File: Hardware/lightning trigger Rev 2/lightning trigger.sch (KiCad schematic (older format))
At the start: 55 parts, among them J1 Conn_01x02, J2 Conn_02x03_Odd_Even, J3 Conn_01x04, J4 PJ-237-6A, J5 PJ-237-6A, J6 USB_OTG, J7 Conn_01x01, J8 Conn_01x01, Q1 Q_Photo_NPN, Q2 BC846B_215, SW1 SW_SPDT, U1 MCP6001, U10 MCP4532, U2 MCP4532, U3 ATMEGA328P-AU, U5 LTV-827S, U6 FS8205, U7 FS312F-G, U8 TP4056, U9 LTV-827S, Y1 Crystal

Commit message: updating resistors and capacitors to be macrofab house parts
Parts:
- removed D1: Green LED, LEDs:LED_0805, symbol Device:LED
- removed D2: Red LED, LEDs:LED_0805, symbol Device:LED
- removed J1: Conn_01x02, Connector_PinHeader_1.00mm:PinHeader_1x02_P1.00mm_Vertical, symbol conn:Conn_01x02
- removed R15, R16, R17: 1k, Resistor_SMD:R_0805_2012Metric, symbol Device:R
- removed R5, R6, R7: 150, Resistor_SMD:R_0805_2012Metric, symbol Device:R
- removed S1: K1-5203UA-01, K1-5203UA-01:K1-5203UA-01, symbol k1-5203ua-01:K1-5203UA-01
- added U4: HM-11, symbol HM-11:HM-11
- C1, C5, C6, C7, C8, C9: footprint Capacitors_SMD:C_0805 -> Capacitor_SMD:C_0603_1608Metric; Manufacturer (none) -> KEMET; Manufacturer P/N 0805B104K250 -> C0603C104J5RACTU; Supplier LCSC -> (none); Supplier P/N C128353 -> (none)
- C10, C4: footprint Capacitors_SMD:C_0805 -> Capacitor_SMD:C_0603_1608Metric; Manufacturer (none) -> KEMET; Manufacturer P/N N/A -> C0603C102J1RACTU; Supplier N/A -> Macrofab; Supplier P/N N/A -> MF-CAP-0603-1nF
- C2, C3: footprint Capacitors_SMD:C_0805 -> Capacitor_SMD:C_0603_1608Metric; Manufacturer (none) -> KEMET; Manufacturer P/N N/A -> C0603C220J1GACTU; Supplier N/A -> Macrofab; Supplier P/N N/A -> MF-CAP-0603-22pF
- J6: footprint USB_Micro:USB_Micro_C77238 -> (none)
- R1: footprint Resistor_SMD:R_0805_2012Metric -> Resistor_SMD:R_0603_1608Metric; Manufacturer (none) -> Panasonic; Manufacturer P/N RMCF0805FT10K0 -> ERJ-3GEYJ103V; Supplier Digikey -> Macrofab; Supplier P/N RMCF0805FT10K0CT-ND -> MF-RES-0603-10K
- R10, R11, R18, R19, R2, R9: footprint Resistor_SMD:R_0805_2012Metric -> Resistor_SMD:R_0603_1608Metric; Manufacturer (none) -> Panasonic; Manufacturer P/N RNCP0603FTD150R -> ERJ-3GEYJ151V; Supplier Digikey -> (none); Supplier P/N RNCP0603FTD150RCT-ND -> (none)
- R12, R13, R14: value 1k -> 2k; footprint Resistor_SMD:R_0805_2012Metric -> Resistor_SMD:R_0603_1608Metric; Manufacturer (none) -> Panasonic; Manufacturer P/N RS-05K1001FT -> ERJ-3GEYJ202V; Supplier LCSC -> (none); Supplier P/N C115316 -> (none)
- R3, R4: value 150 -> 10k; footprint Resistor_SMD:R_0805_2012Metric -> Resistor_SMD:R_0603_1608Metric; Manufacturer (none) -> Panasonic; Manufacturer P/N (none) -> ERJ-3GEYJ103V; Supplier (none) -> Macrofab; Supplier P/N (none) -> MF-RES-0603-10K
- R8: footprint Resistor_SMD:R_0805_2012Metric -> Resistor_SMD:R_0603_1608Metric; Manufacturer (none) -> Panasonic; Manufacturer P/N ERJ-6ENF1603V -> ERJ-3GEYJ164V; Supplier Digikey -> (none); Supplier P/N P160KCCT-ND -> (none)
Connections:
- net labels added: 3.3V, ~CHARGE, ~STDBY
- net labels removed: CENTER, DOWN, LEFT, RIGHT, UP
- wire segments 231 -> 210
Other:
- moved on the sheet: C2, C3, J4, R18, R19, U3, Y1

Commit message: more schematic updates with new components
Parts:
- removed Q2: BC846B_215, digikey-footprints:SOT-23-3, symbol lightning-trigger-rescue:BC846B_215-dk_Transistors-Bipolar-BJT-Single
- removed U5, U9: LTV-827S, LTV-827S-TA1:LTV-827S-TA1, symbol ltv-827s:LTV-827S
- added J1, J9: PJ-237-6A, PJ-237-6A:PJ-237-6A, symbol pj-237-6a:PJ-237-6A
- added Q2: MMBT3904, Package_TO_SOT_SMD:SOT-23, symbol Transistor_BJT:MMBT3904
- added R15, R5, R6, R7: 150, Resistor_SMD:R_0603_1608Metric, symbol Device:R
- added U5, U9: TLP291-4, Package_SO:SOIC-16_4.55x10.3mm_P1.27mm, symbol Isolator:TLP291-4
- J6: footprint (none) -> USB:USB_Micro_C77238; Manufacturer P/N N/A -> (none)
- Q1: Manufacturer (none) -> OSRAM Opto Semiconductors
- U1, U3: Manufacturer (none) -> Microchip Technology
- U10, U2: Manufacturer (none) -> Toshiba
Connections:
- net labels added: FOCUS1, FOCUS3, FOCUS4, SHUTTER1, SHUTTER3, SHUTTER4
- wire segments 210 -> 250
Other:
- moved on the sheet: J4, J5, R10, R18, R19, R9

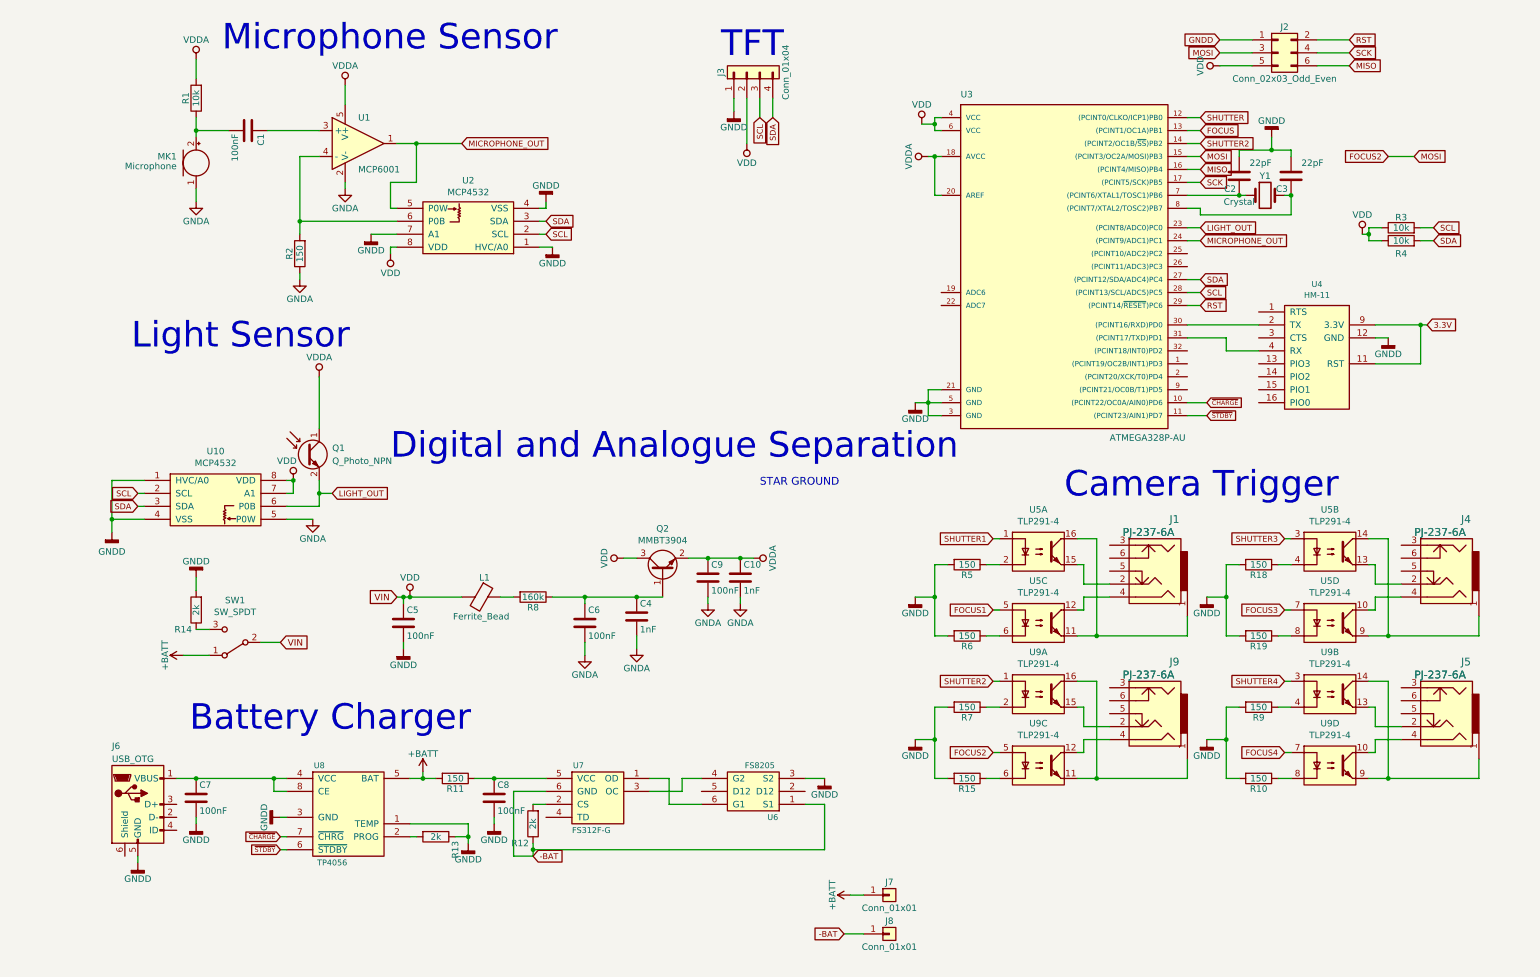
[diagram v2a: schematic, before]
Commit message: added battery monitor circuitry, and power mux for switching between charging and battery power
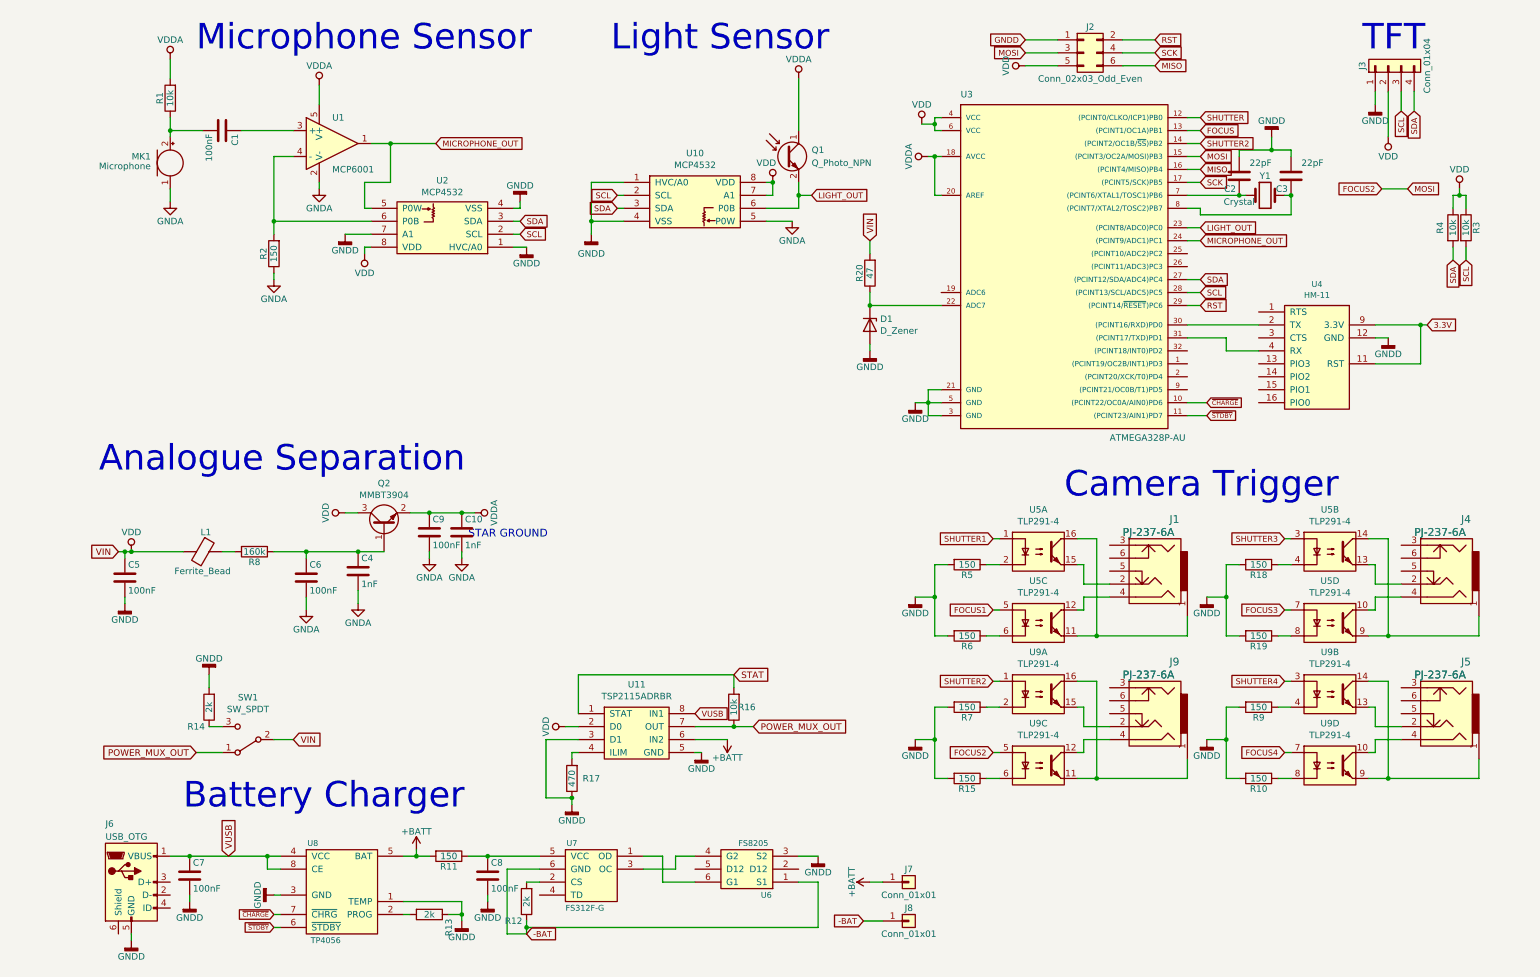
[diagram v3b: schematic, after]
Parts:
- added D1: D_Zener, Diode_SMD:SC-90A, symbol Device:D_Zener
- added R16: 10k, Resistor_SMD:R_0603_1608Metric, symbol Device:R
- added R17: 470, Resistor_SMD:R_0603_1608Metric, symbol Device:R
- added R20: 47, Resistor_SMD:R_0603_1608Metric, symbol Device:R
- added U11: TSP2115ADRBR, Package_SON:SON-8-1EP_3x2mm_P0.5mm_EP1.4x1.6mm, symbol texas2:TSP2115ADRBR
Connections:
- net +BATT: now also U11.6 (IN2); no longer SW1.1 (A)
- net GNDD: now also D1.2 (A), R17.1, U11.3 (D1), U11.5 (GND)
- net VDD: now also R20.2, U11.2 (D0)
- net at U3.22 (ADC7): now also D1.1 (K), R20.1
- net VUSB: now reaches C7.1, J6.1 (VBUS), U8.4 (VCC), U8.8 (CE)
- net VUSB: now also U11.8 (IN1)
- new net: R17.2, U11.4 (ILIM)
- new net POWER_MUX_OUT: R16.1, SW1.1 (A), U11.7 (OUT)
- new net STAT: R16.2, U11.1 (STAT)
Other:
- note added: "Analogue Separation"
- note removed: "Digital and Analogue Separation"
- moved on the sheet: C1, C10, C4, C5, C6, C7, C8, C9, J2, J3, J6, J7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

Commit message: more schematic updates for power mux
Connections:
- net +BATT: now also SW1.1 (A); no longer U11.6 (IN2)
- net STAT: now also U3.19 (ADC6)
- net VDD: now also R16.1, U11.7 (OUT); no longer R20.2, SW1.2 (B)
- removed net POWER_MUX_OUT: R16.1, SW1.1 (A), U11.7 (OUT)
- new net VIN: R20.2, SW1.2 (B), U11.6 (IN2)
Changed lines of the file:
@@
 	1    0    0    -1
 $EndComp
-Text GLabel 650  4600 0    50   Input ~ 0
-VIN
 Text GLabel 2000 6050 2    50   Input ~ 0
 VIN
@@
 Text GLabel 5100 5850 2    45   Input ~ 0
 VUSB
-$Comp
-L power:+BATT #PWR010
-U 1 1 5CF9BB53
-P 5350 6050
-F 0 "#PWR010" H 5350 5900 50  0001 C CNN
-F 1 "+BATT" H 5350 6190 50  0000 C CNN
-F 2 "" H 5350 6050 50  0001 C CNN
-F 3 "" H 5350 6050 50  0001 C CNN
-	1    5350 6050
-	-1   0    0    1
-$EndComp
 Text GLabel 5550 5950 2    50   Input ~ 0
 POWER_MUX_OUT
@@
 	3950 6500 4150 6500
 Connection ~ 4150 6500
-Text GLabel 1250 6150 0    50   Input ~ 0
-POWER_MUX_OUT
 $Comp
 L power:VDD #PWR09
@@
 Wire Wire Line
 	7000 2700 6450 2700
+$Comp
+L power:+BATT #PWR?
+U 1 1 5D2369AE
+P 1250 6150
+F 0 "#PWR?" H 1250 6000 50  0001 C CNN
+F 1 "+BATT" H 1250 6290 50  0000 C CNN
+F 2 "" H 1250 6150 50  0001 C CNN
+F 3 "" H 1250 6150 50  0001 C CNN
+	1    1250 6150
+	0    -1   -1   0
+$EndComp
+Text GLabel 5350 6050 2    50   Input ~ 0
+VIN
+Text GLabel 650  4600 0    50   Input ~ 0
+POWER_MUX_OUT
+Text GLabel 6900 2600 0    50   Input ~ 0
+STAT
+Wire Wire Line
+	6900 2600 7000 2600
 $EndSCHEMATC

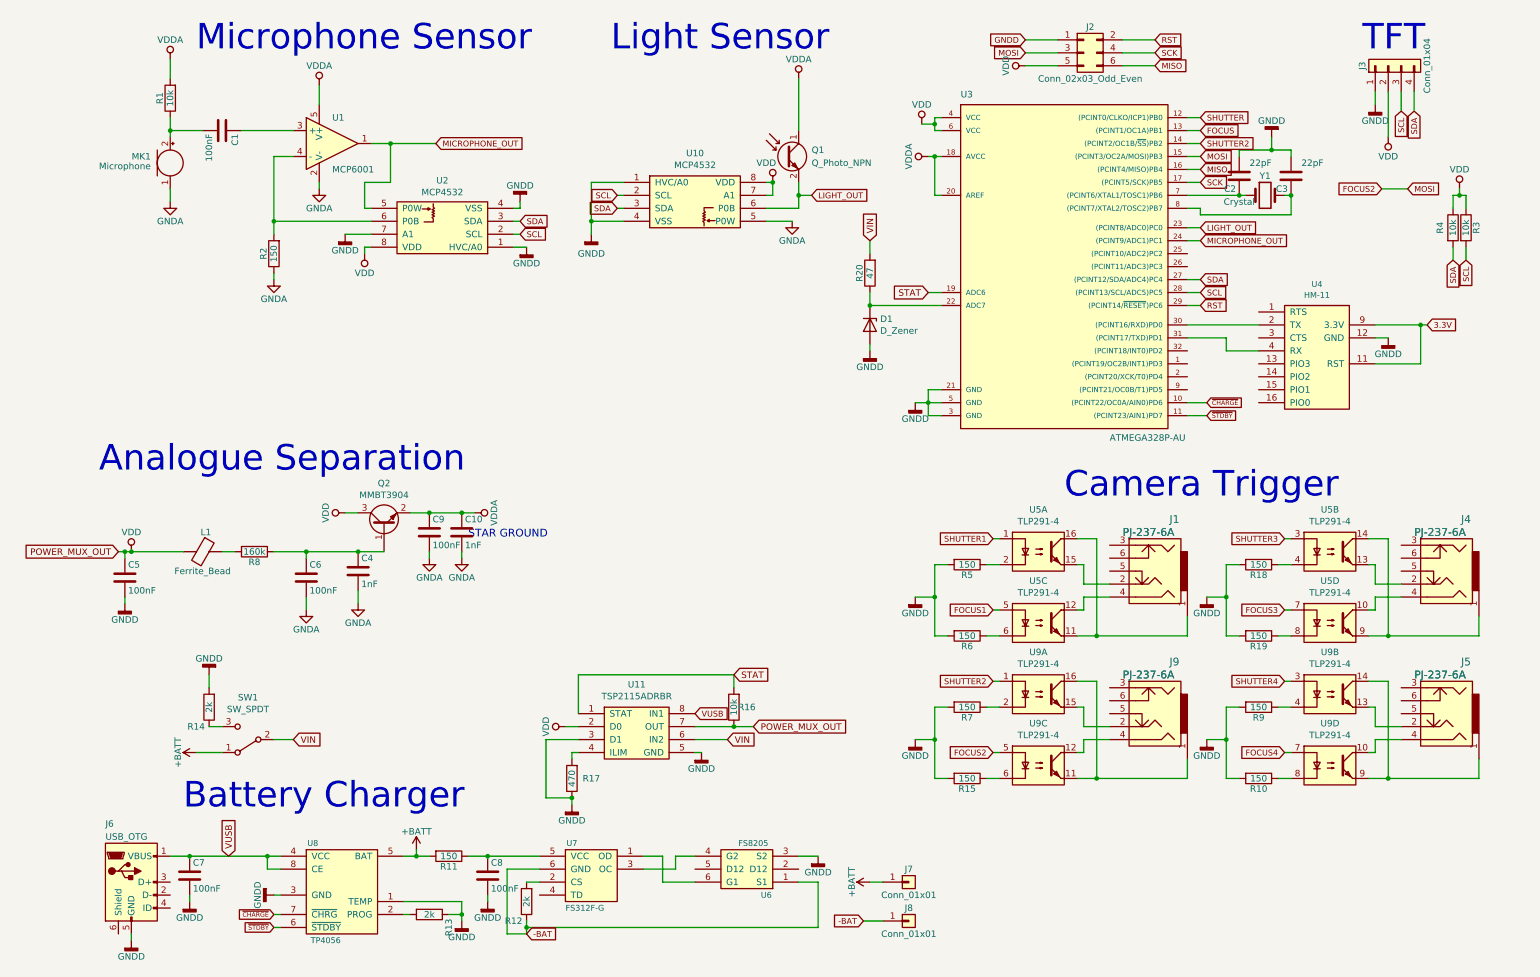
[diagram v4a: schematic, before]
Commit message: added logic conversion for HM-11 RX module
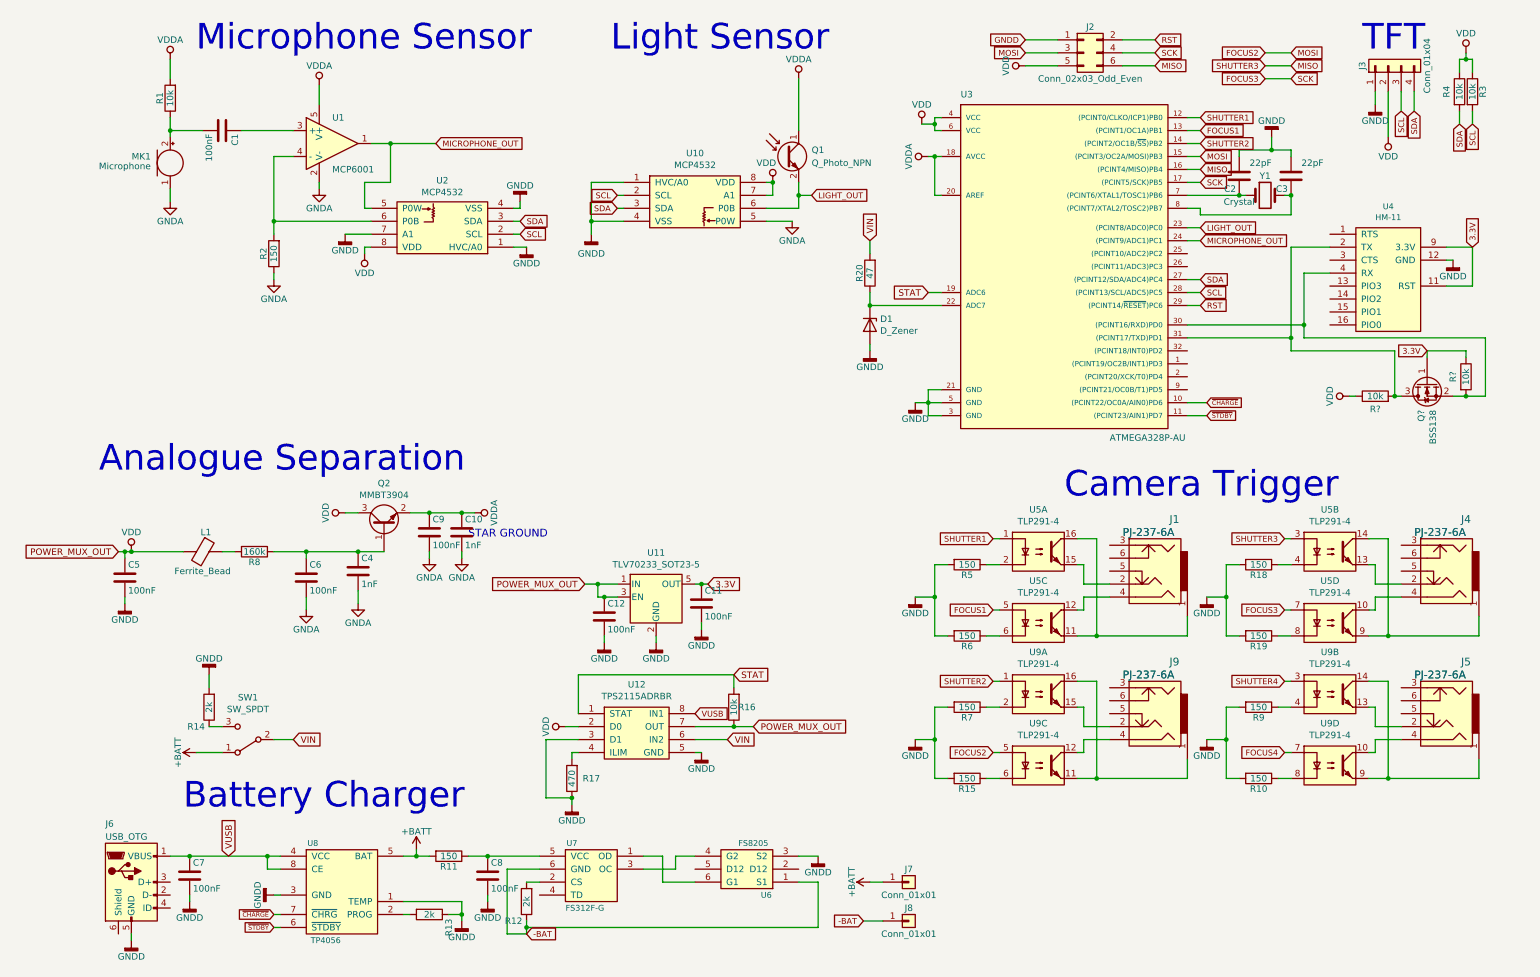
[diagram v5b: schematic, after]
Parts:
- removed U11: TSP2115ADRBR, Package_SON:SON-8-1EP_3x2mm_P0.5mm_EP1.4x1.6mm, symbol texas2:TSP2115ADRBR
- added C11, C12: 100nF, Capacitor_SMD:C_0603_1608Metric, symbol Device:C
- added Q?: BSS138, Package_TO_SOT_SMD:SOT-23, symbol Transistor_FET:BSS138
- added R? (x2): 10k, Resistor_SMD:R_0603_1608Metric, symbol Device:R
- added U11: TLV70233_SOT23-5, Package_TO_SOT_SMD:SOT-23-5, symbol Regulator_Linear:TLV70233_SOT23-5
- added U12: TPS2115ADRBR, Package_SON:SON-8-1EP_3x2mm_P0.5mm_EP1.4x1.6mm, symbol texas2:TPS2115ADRBR
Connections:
- net FOCUS is gone; now on net FOCUS1: U3.13 ((PCINT1/OC1A)PB1)
- net SCK is gone; now on net FOCUS3: J2.4 (Pin_4), U3.17 ((PCINT5/SCK)PB5)
- net SHUTTER is gone; now on net SHUTTER1: U3.12 ((PCINT0/CLKO/ICP1)PB0)
- net SHUTTER3 is gone; now on net MISO: U5.3
- net 3.3V: now also C11.1, Q?.1 (G), R?.1, U11.5 (OUT)
- net GNDD: now also C11.2, C12.2, U11.2 (GND), U12.3 (D1), U12.5 (GND)
- net STAT: now also U12.1 (STAT)
- net VDD: now also C12.1, R?.1, U11.1 (IN), U11.3 (EN), U12.2 (D0), U12.7 (OUT)
- net VIN: now also U12.6 (IN2)
- net VUSB: now also U12.8 (IN1)
- net at U3.30 ((PCINT16/RXD)PD0): now also U4.4 (RX), Q?.2 (S), R?.2; no longer U4.2 (TX)
- net at U3.31 ((PCINT17/TXD)PD1): now also U4.2 (TX), Q?.3 (D), R?.2; no longer U4.4 (RX)
- net at R17.2: now also U12.4 (ILIM)
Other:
- moved on the sheet: R3, R4, U4

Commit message: more changes to rev 2 schematic
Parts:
- U4: footprint (none) -> HM-11:HM-11
- gave numbers to parts that had none: 3
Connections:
- net at J1.4, U5.12: now also J1.3
- net at J9.4, U9.12: now also J9.3
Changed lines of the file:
@@
 F 0 "U4" H 10450 3064 45  0000 C CNN
 F 1 "HM-11" H 10450 2980 45  0000 C CNN
-F 2 "" H 10400 2500 45  0001 C CNN
+F 2 "HM-11:HM-11" H 10400 2500 45  0001 C CNN
 F 3 "" H 10400 2500 45  0001 C CNN
 F 4 "HM-11" H 550 -600 50  0001 C CNN "Manufacturer P/N"
@@
 	8100 5050 8100 4950
 Wire Wire Line
-	8100 4950 8300 4950
+	8100 4950 8250 4950
 Wire Wire Line
 	8050 4700 8100 4700
@@
 	8100 6150 8100 6050
 Wire Wire Line
-	8100 6050 8300 6050
+	8100 6050 8250 6050
 Wire Wire Line
 	8050 5800 8100 5800
@@
 $EndComp
 $Comp
-L Transistor_FET:BSS138 Q?
+L Transistor_FET:BSS138 Q3
 U 1 1 5CCA242E
 P 10750 3300
-F 0 "Q?" H 10956 3346 50  0000 L CNN
+F 0 "Q3" H 10956 3346 50  0000 L CNN
 F 1 "BSS138" H 10956 3255 50  0000 L CNN
 F 2 "Package_TO_SOT_SMD:SOT-23" H 10950 3225 50  0001 L CIN
@@
 $EndComp
 $Comp
-L Device:R R?
+L Device:R R22
 U 1 1 5CCA2588
 P 10350 3400
-F 0 "R?" V 10250 3400 50  0000 C CNN
+F 0 "R22" V 10250 3400 50  0000 C CNN
 F 1 "10k" V 10350 3400 50  0000 C CNN
 F 2 "Resistor_SMD:R_0603_1608Metric" V 10280 3400 50  0001 C CNN
@@
 $EndComp
 $Comp
-L power:VDD #PWR?
+L power:VDD #PWR0125
 U 1 1 5CCB8827
 P 10150 3400
-F 0 "#PWR?" H 10150 3250 50  0001 C CNN
+F 0 "#PWR0125" H 10150 3250 50  0001 C CNN
 F 1 "VDD" H 10150 3550 50  0000 C CNN
 F 2 "" H 10150 3400 50  0001 C CNN
@@
 	10500 3400 10550 3400
 $Comp
-L Device:R R?
+L Device:R R21
 U 1 1 5CDCBE77
 P 11050 3250
-F 0 "R?" V 10950 3250 50  0000 C CNN
+F 0 "R21" V 10950 3250 50  0000 C CNN
 F 1 "10k" V 11050 3250 50  0000 C CNN
 F 2 "Resistor_SMD:R_0603_1608Metric" V 10980 3250 50  0001 C CNN
@@
 Wire Wire Line
 	8900 2950 9700 2950
+Wire Wire Line
+	8300 5650 8250 5650
+Wire Wire Line
+	8250 5650 8250 6050
+Connection ~ 8250 6050
+Wire Wire Line
+	8250 6050 8300 6050
+Wire Wire Line
+	8300 4550 8250 4550
+Wire Wire Line
+	8250 4550 8250 4950
+Connection ~ 8250 4950
+Wire Wire Line
+	8250 4950 8300 4950
 $EndSCHEMATC
